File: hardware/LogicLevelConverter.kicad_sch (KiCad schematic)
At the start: 9 parts, among them Q1 2N7002NXAKR, Q501 NMOS, Q502 NMOS

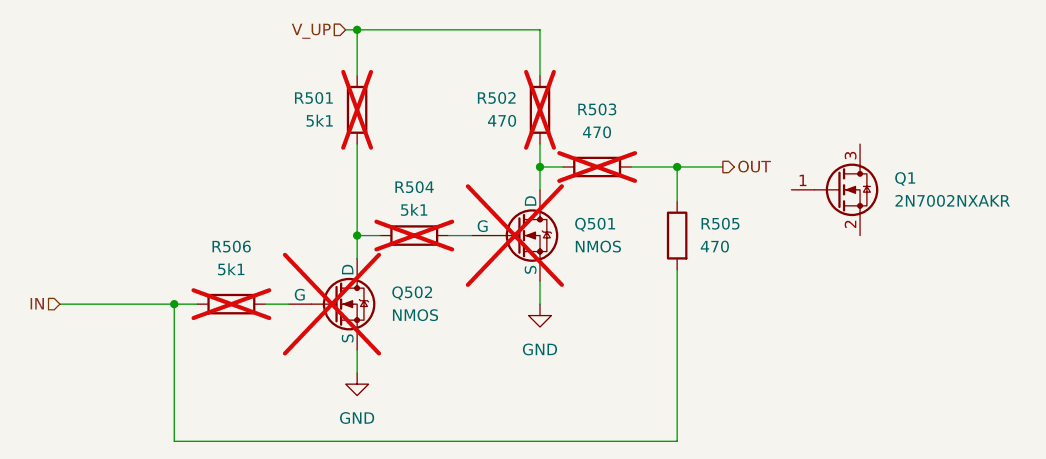
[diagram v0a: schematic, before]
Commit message: Optimized BOM and added netties
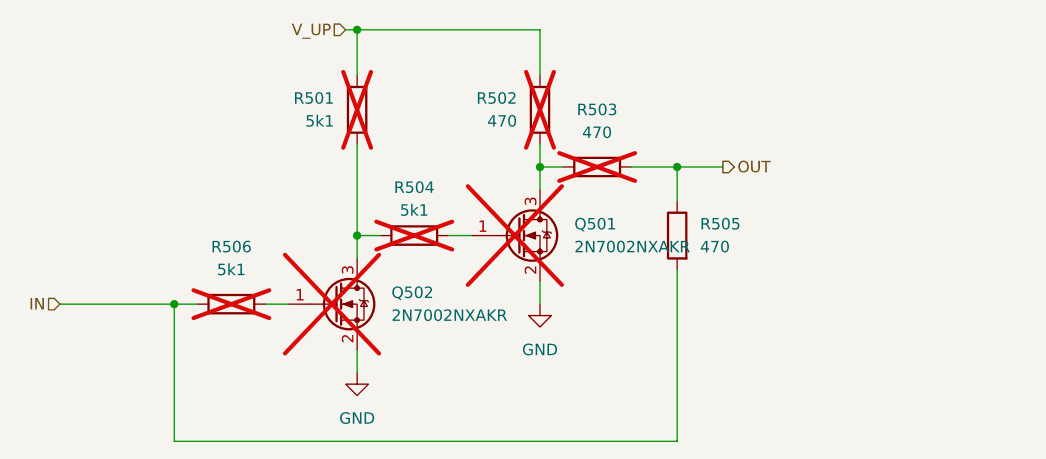
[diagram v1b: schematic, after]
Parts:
- removed Q1: 2N7002NXAKR, Package_TO_SOT_SMD:SOT-23-3, symbol Transistor_FET:2N7002
- removed Q501, Q502: NMOS, symbol Simulation_SPICE:NMOS
- added Q501, Q502: 2N7002NXAKR, Package_TO_SOT_SMD:SOT-23-3, symbol glowbuck:2N7002NXAKR
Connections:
- net GND: now also Q501.2 (S), Q502.2 (S)
- net at R502.1, R503.2: now also Q501.3 (D)
- net at R501.1, R504.2: now also Q502.3 (D)
- net at R506.1: now also Q502.1 (G)
- net at R504.1: now also Q501.1 (G)
